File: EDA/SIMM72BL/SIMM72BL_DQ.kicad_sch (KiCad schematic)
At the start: 75 parts, among them U2 74HC14, U3 74HC14, U4 74HC14, U5 74HC14, U6 74HC14, U7 74HC14

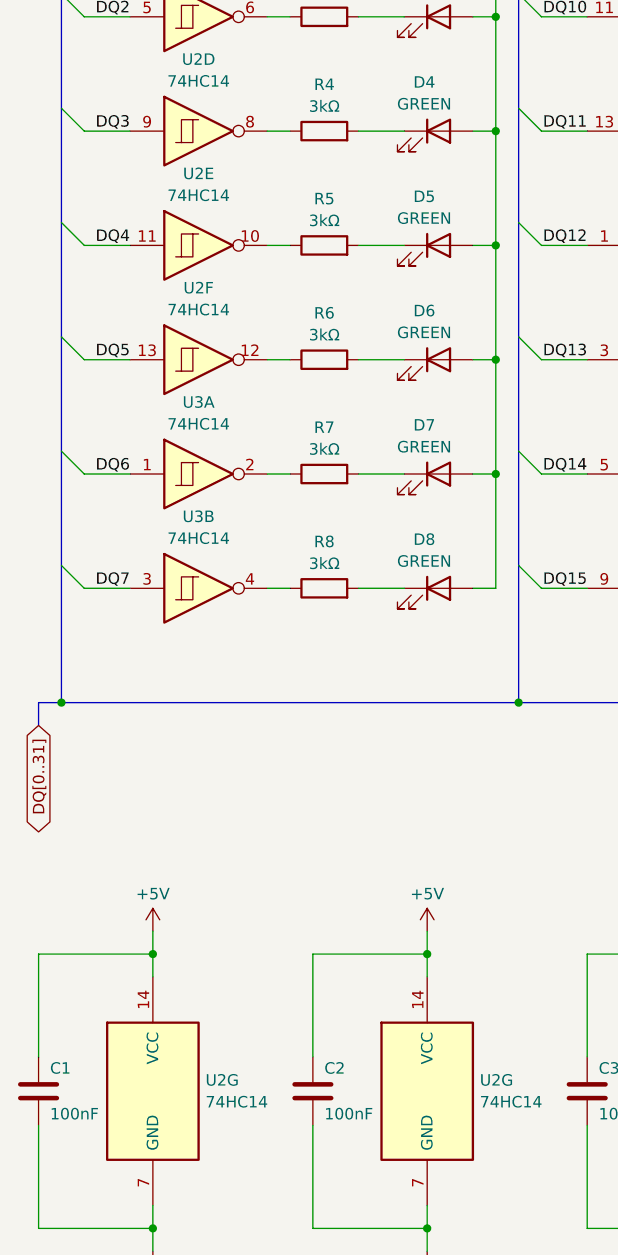
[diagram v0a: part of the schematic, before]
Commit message: SIMM72BL v1.2: fixed decoupling caps footprint & silkscreen
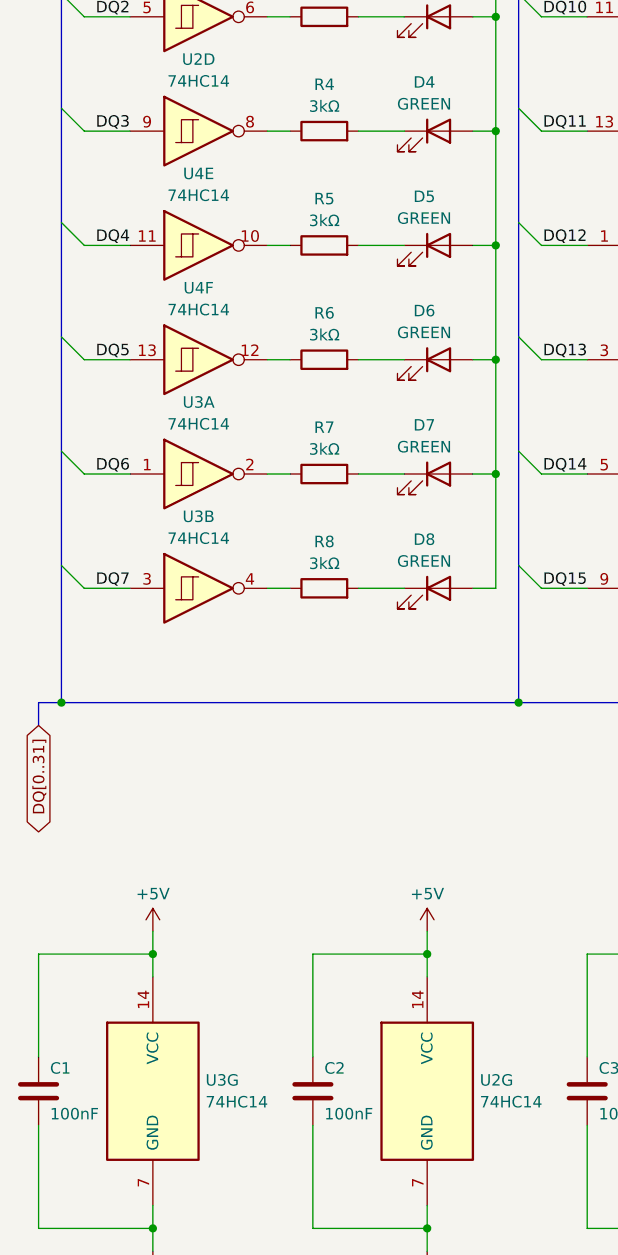
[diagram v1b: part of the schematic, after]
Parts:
- renumbered U2 to U3, U2 to U4
